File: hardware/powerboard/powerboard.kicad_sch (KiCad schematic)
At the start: 66 parts, among them J1 USB_B_Micro, J10 5V Header, J11 3V3 Header, J2 Boot, J3 Power, J4 Display, J5 Debug, J6 SPI_1, J7 UART_0, J8 I2C_0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

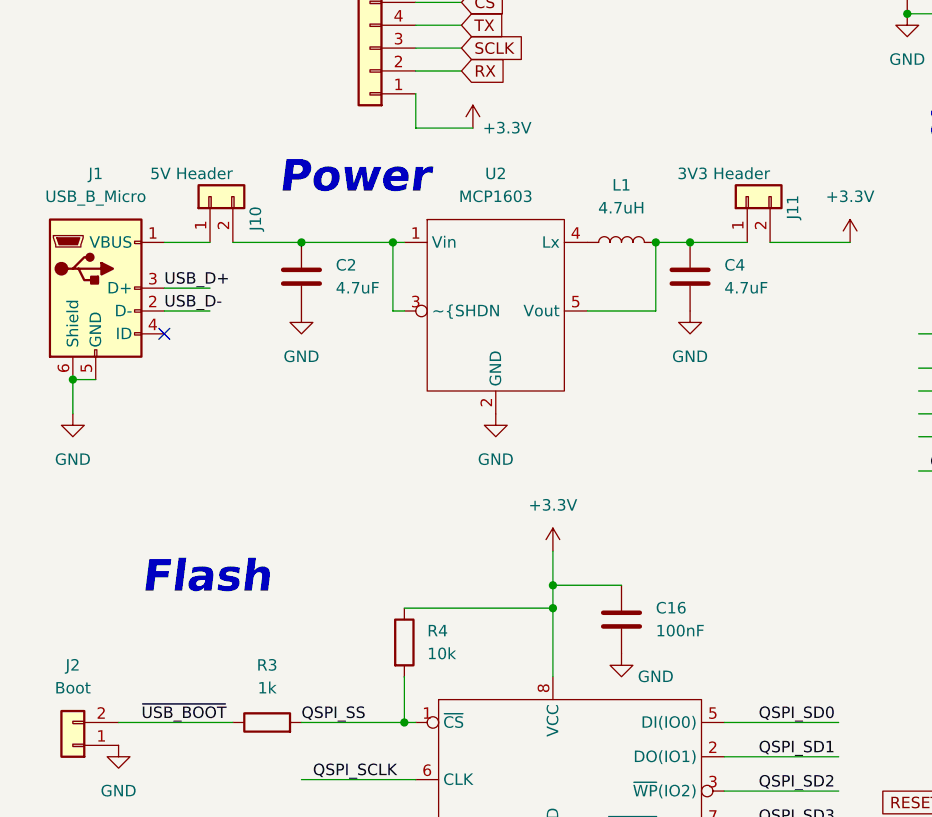
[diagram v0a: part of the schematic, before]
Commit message: JLC Capabilities Double Checked
Confirmed JLC Capabilities with Design Rules
CHECK SILKSCREEN RULES
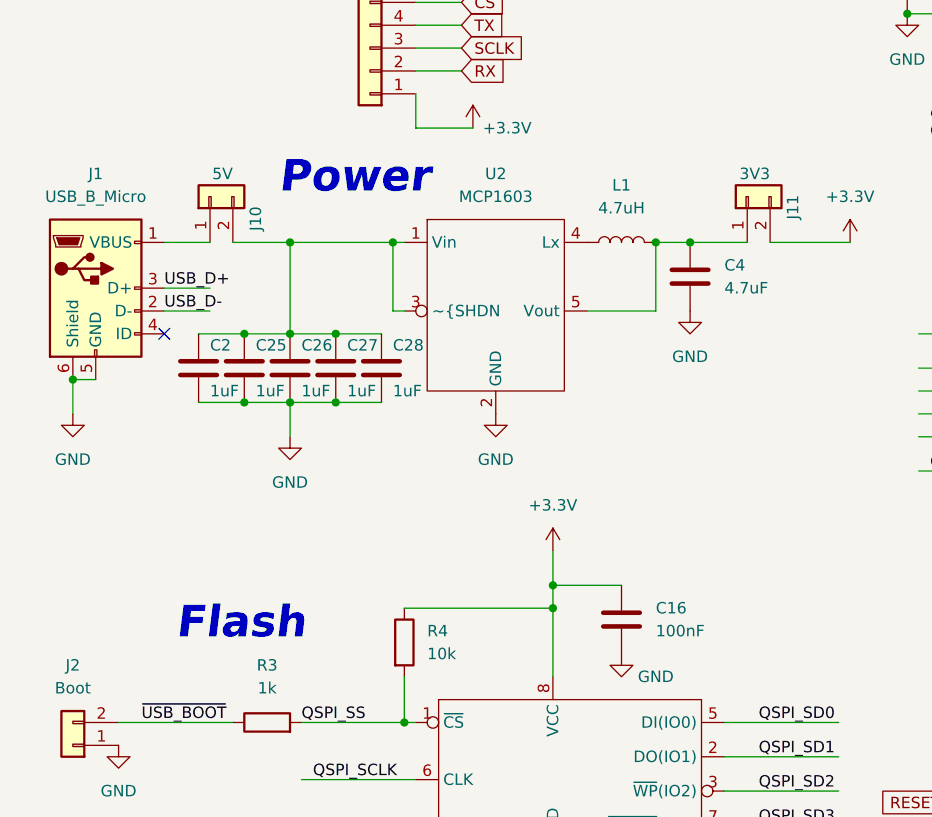
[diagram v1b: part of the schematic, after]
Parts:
- added C25, C26, C27, C28: 1uF, Capacitor_SMD:C_0805_2012Metric, symbol Device:C
- C2: value 4.7uF -> 1uF; footprint Capacitor_SMD:C_0603_1608Metric -> Capacitor_SMD:C_0805_2012Metric
- J10: value 5V Header -> 5V
- J11: value 3V3 Header -> 3V3
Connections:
- net GND: now also C25.2, C26.2, C27.2, C28.2
- net at C2.1, J10.2 (Pin_2), U2.1 (Vin)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: now also C25.1, C26.1, C27.1, C28.1

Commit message: MIDI Messages now only sent on Keypress
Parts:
- C4: footprint Capacitor_SMD:C_0603_1608Metric -> Capacitor_SMD:C_0805_2012Metric
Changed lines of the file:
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@@
       (effects (font (size 1.27 1.27)) (justify left))
     )
-    (property "Footprint" "Capacitor_SMD:C_0603_1608Metric" (id 2) (at 89.8652 69.85 0)
+    (property "Footprint" "Capacitor_SMD:C_0805_2012Metric" (id 2) (at 89.8652 69.85 0)
       (effects (font (size 1.27 1.27)) hide)
     )
@@
     )
     (path "/707b3643-99d8-4514-bbf8-587962bdcb4f"
-      (reference "C4") (unit 1) (value "4.7uF") (footprint "Capacitor_SMD:C_0603_1608Metric")
+      (reference "C4") (unit 1) (value "4.7uF") (footprint "Capacitor_SMD:C_0805_2012Metric")
     )
     (path "/62a559f3-0287-407e-b429-1597a5ab7b86"

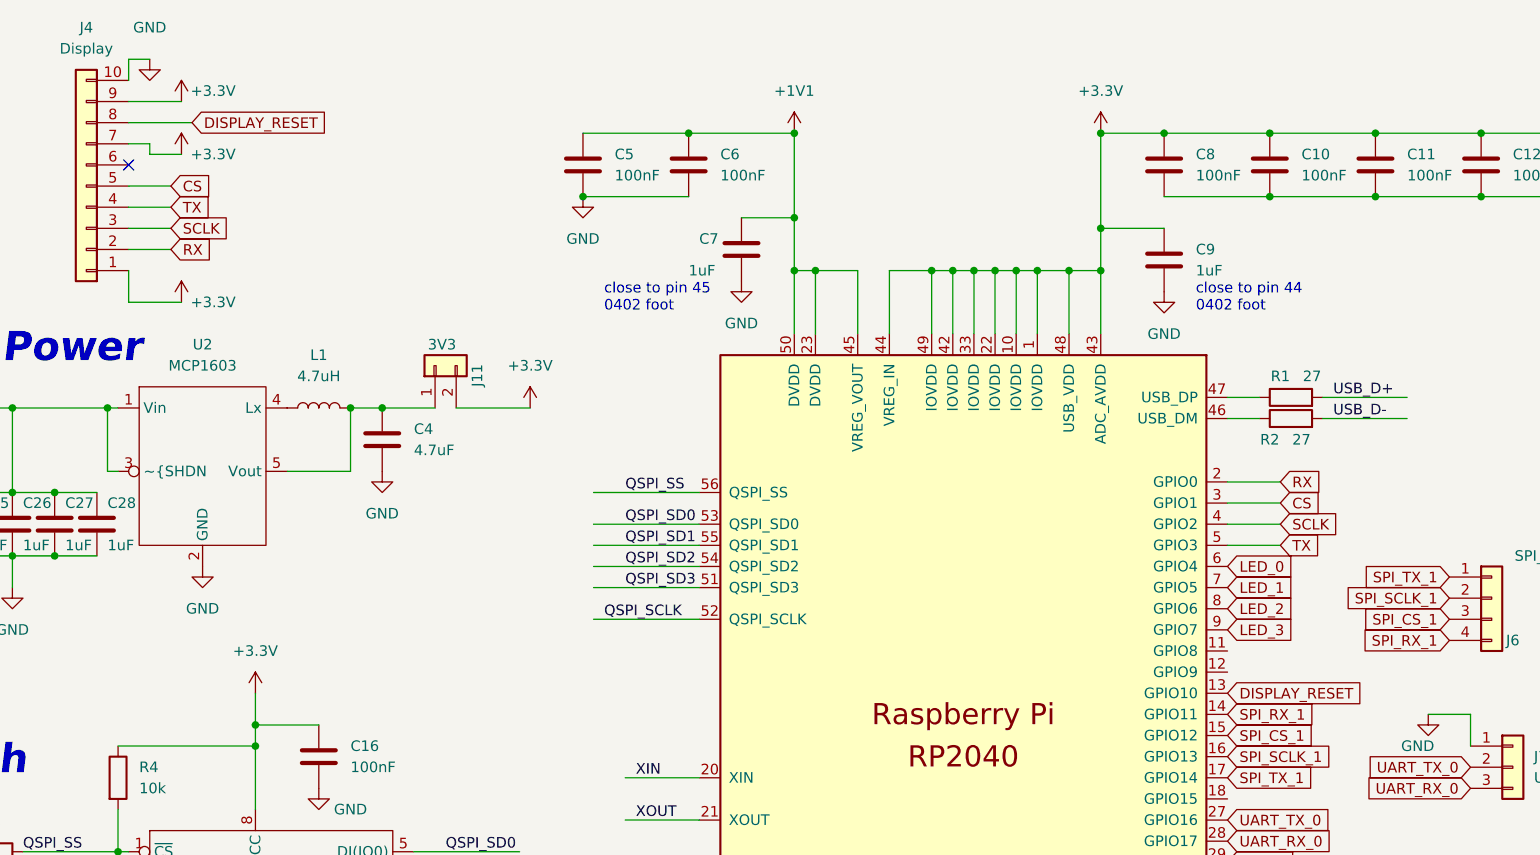
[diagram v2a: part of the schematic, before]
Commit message: GPIO Added for TFT_DC Display Pin
Connected GPIO 10 to TFT_DC Pin on Display Header
DISPLAY_RESET is now Connected to GPIO 9
pins.h updated accordingly
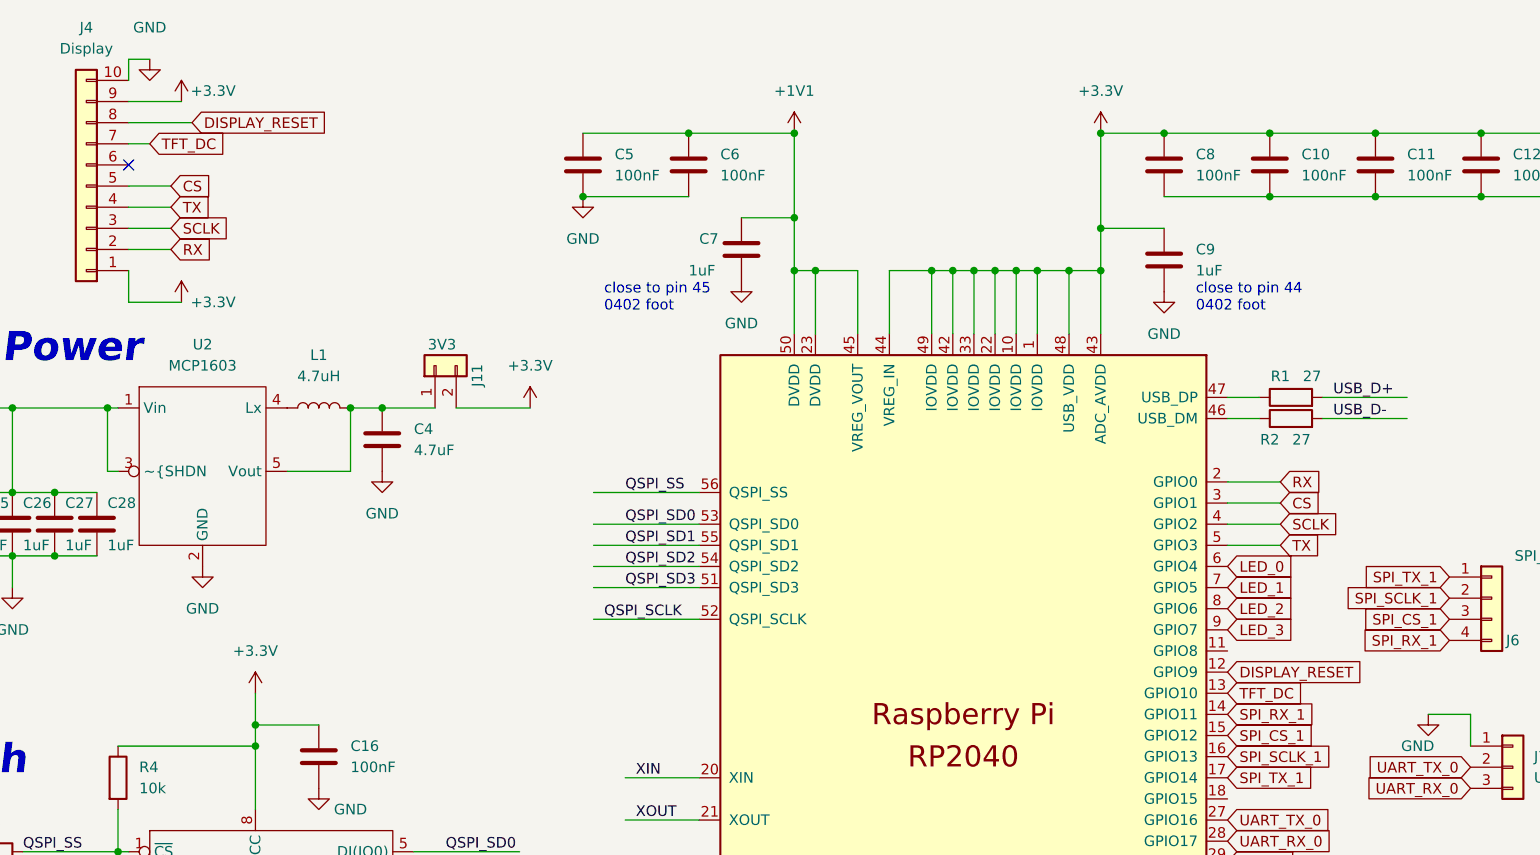
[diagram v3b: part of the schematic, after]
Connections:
- net +3.3V: no longer J4.7 (Pin_7)
- net DISPLAY_RESET: now also U3.12 (GPIO9); no longer U3.13 (GPIO10)
- new net TFT_DC: J4.7 (Pin_7), U3.13 (GPIO10)
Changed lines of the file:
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@@
-    (stroke (width 0) (type default) (color 0 0 0 0))
-  )
-  (wire (pts (xy 64.77 31.75) (xy 60.96 31.75))
     (stroke (width 0) (type default) (color 0 0 0 0))
   )
@@
   )
   (wire (pts (xy 22.86 152.4) (xy 27.94 152.4))
-    (stroke (width 0) (type default) (color 0 0 0 0))
-  )
-  (wire (pts (xy 60.96 31.75) (xy 60.96 30.48))
     (stroke (width 0) (type default) (color 0 0 0 0))
   )
@@
     )
   )
-  (global_label "DISPLAY_RESET" (shape input) (at 190.5 96.52 0) (fields_autoplaced)
-    (effects (font (size 1.27 1.27)) (justify left))
-    (property "Intersheet References" "${INTERSHEET_REFS}" (id 0) (at 207.1855 96.4406 0)
+  (global_label "DISPLAY_RESET" (shape input) (at 190.5 93.98 0) (fields_autoplaced)
+    (effects (font (size 1.27 1.27)) (justify left))
+    (property "Intersheet References" "${INTERSHEET_REFS}" (id 0) (at 207.1855 93.9006 0)
+      (effects (font (size 1.27 1.27)) (justify left) hide)
+    )
+  )
+  (global_label "TFT_DC" (shape input) (at 60.96 30.48 0) (fields_autoplaced)
+    (effects (font (size 1.27 1.27)) (justify left))
+    (property "Intersheet References" "${INTERSHEET_REFS}" (id 0) (at 69.9045 30.4006 0)
       (effects (font (size 1.27 1.27)) (justify left) hide)
     )
@@
     (property "Intersheet References" "${INTERSHEET_REFS}" (id 0) (at 16.8788 177.7206 0)
       (effects (font (size 1.27 1.27)) (justify right) hide)
+    )
+  )
+  (global_label "TFT_DC" (shape input) (at 190.5 96.52 0) (fields_autoplaced)
+    (effects (font (size 1.27 1.27)) (justify left))
+    (property "Intersheet References" "${INTERSHEET_REFS}" (id 0) (at 199.4445 96.4406 0)
+      (effects (font (size 1.27 1.27)) (justify left) hide)
     )
   )
@@
     (pin "2")
   )
-  (symbol (lib_id "power:+3.3V") (at 64.77 31.75 0) (unit 1)
-    (in_bom yes) (on_board yes)
-    (property "Reference" "#PWR06" (id 0) (at 64.77 35.56 0)
-      (effects (font (size 1.27 1.27)) hide)
-    )
-    (property "Value" "+3.3V" (id 1) (at 68.58 31.75 0))
-    (property "Footprint" "" (id 2) (at 64.77 31.75 0)
-      (effects (font (size 1.27 1.27)) hide)
-    )
-    (property "Datasheet" "" (id 3) (at 64.77 31.75 0)
-      (effects (font (size 1.27 1.27)) hide)
-    )
-    (pin "1")
-  )
   (symbol (lib_id "power:+3.3V") (at 34.29 22.86 0) (unit 1)
     (in_bom yes) (on_board yes) (fields_autoplaced)
@@
       (reference "#PWR05") (unit 1) (value "GND") (footprint "")
     )
-    (path "/f8107bfa-8926-48fc-a59a-d44657ce0461"
-      (reference "#PWR06") (unit 1) (value "+3.3V") (footprint "")
-    )
     (path "/550650b9-9aa6-4198-b86a-a5c8675143c2"

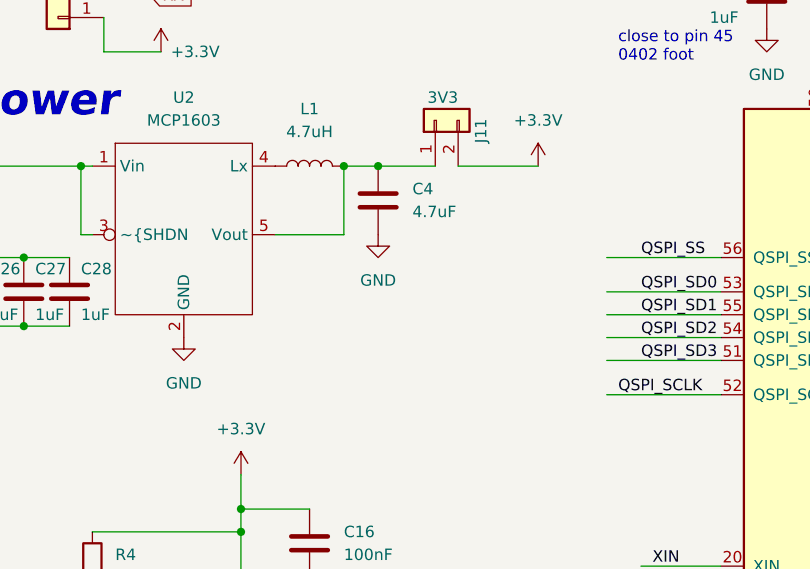
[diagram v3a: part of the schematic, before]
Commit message: powerboard adjustments, bom added
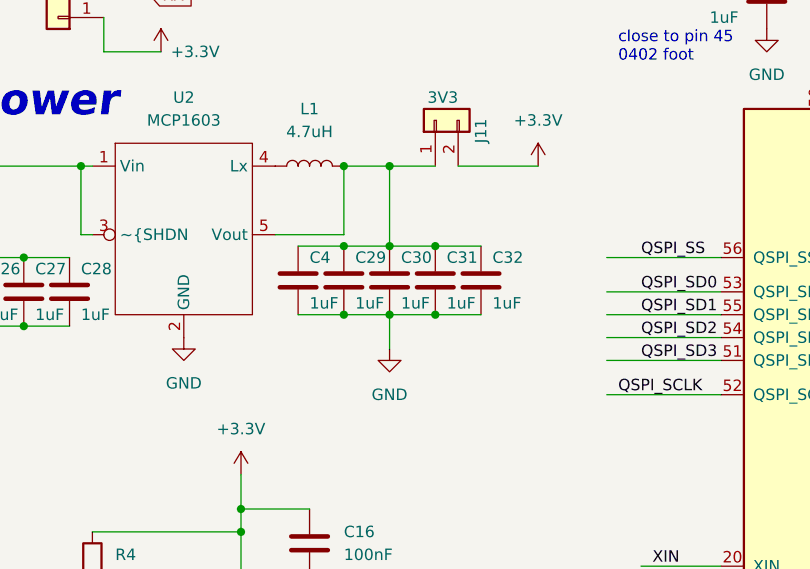
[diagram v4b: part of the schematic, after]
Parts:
- added C29, C30, C31, C32: 1uF, Capacitor_SMD:C_0805_2012Metric, symbol Device:C
- C4: value 4.7uF -> 1uF
- J7: footprint Connector_PinSocket_2.54mm:PinSocket_1x03_P2.54mm_Vertical -> Connector_PinHeader_2.54mm:PinHeader_1x03_P2.54mm_Vertical
- J8, J9: footprint Connector_PinSocket_2.54mm:PinSocket_1x04_P2.54mm_Vertical -> Connector_PinHeader_2.54mm:PinHeader_1x04_P2.54mm_Vertical
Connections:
- net GND: now also C29.2, C30.2, C31.2, C32.2
- net at C4.1, J11.1 (Pin_1), L1.2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: now also C29.1, C30.1, C31.1, C32.1

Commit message: Powerboard Output Files Pt.1
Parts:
- C1, C10, C11, C12, C13, C14, C15, C16, C23, C24, C5, C6, C8: LCSC (none) -> C307331
- C17, C18: LCSC (none) -> C1658
- C19, C20, C21: LCSC (none) -> C1588
- C2, C25, C26, C27, C28, C29, C30, C31, C32, C4: LCSC (none) -> C28323
- C22: LCSC (none) -> C440198
- C3: footprint Capacitor_SMD:C_0603_1608Metric -> Capacitor_SMD:C_0402_1005Metric; LCSC (none) -> C307331
- C7, C9: LCSC (none) -> C307413
- D1, D2, D3, D4: LCSC (none) -> C87326
- J1: LCSC (none) -> C132563
- J10, J11, J2: LCSC (none) -> C2905434
- J3: LCSC (none) -> C2905424
- J4: LCSC (none) -> C2905488
- J5, J7: LCSC (none) -> C2932698
- J6: LCSC (none) -> C492412
- J8, J9: LCSC (none) -> C2905345
- L1: LCSC (none) -> C701275
- R1, R2: LCSC (none) -> C25100
- R10, R11, R3, R5, R6, R7, R8, R9: LCSC (none) -> C21190
- R12, R13, R14, R4: LCSC (none) -> C25804
- R15, R16, R17, R18: LCSC (none) -> C23138
- SW1, SW2, SW3: LCSC (none) -> C428628
- SW4: LCSC (none) -> C278348
- U2: LCSC (none) -> C150803
- U3: LCSC (none) -> C9900024873
- U4: LCSC (none) -> C2613930
- Y1: LCSC (none) -> C133334
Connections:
- net +3.3V: now also C29.1, C30.1, C31.1, C32.1, C4.1, J11.1 (Pin_1), L1.2, U2.5 (Vout)
- no-connect marks 3 -> 7
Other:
- company: (none) -> Landyn Francis & Jacob Mealey
- title: (none) -> MIDI Keyboard: Brain Board

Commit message: Gerbers and pick and place generated
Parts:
- removed J3: Power, Connector_PinHeader_2.54mm:PinHeader_1x02_P2.54mm_Horizontal, symbol Connector_Generic:Conn_01x02
- removed J6: SPI_1, Connector_PinHeader_2.54mm:PinHeader_1x04_P2.54mm_Horizontal, symbol Connector_Generic:Conn_01x04
- added J3: Keysboard Header, Connector_PinHeader_2.54mm:PinHeader_1x06_P2.54mm_Horizontal, symbol Connector_Generic:Conn_01x06
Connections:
- net +3.3V: now also J3.2 (Pin_2)
- net GND: now also J3.1 (Pin_1)
- net SPI_CS_1: now also J3.5 (Pin_5)
- net SPI_RX_1: now also J3.6 (Pin_6)
- net SPI_SCLK_1: now also J3.4 (Pin_4)
- net SPI_TX_1: now also J3.3 (Pin_3)

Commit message: Footprint adjusted for W25QJVSIM FLASH
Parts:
- J8, J9: LCSC C2905345 -> C2905435
- U4: footprint Package_SO:SOIC-8_7.5x5.85mm_P1.27mm -> Package_SO:SOIC-8W_5.3x5.3mm_P1.27mm
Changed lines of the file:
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@@
       (effects (font (size 1.27 1.27)) hide)
     )
-    (property "LCSC" "C2905345" (id 4) (at 224.79 151.13 0)
+    (property "LCSC" "C2905435" (id 4) (at 224.79 151.13 0)
       (effects (font (size 1.27 1.27)) hide)
     )
@@
       (effects (font (size 1.27 1.27)) hide)
     )
-    (property "LCSC" "C2905345" (id 4) (at 228.6 125.73 0)
+    (property "LCSC" "C2905435" (id 4) (at 228.6 125.73 0)
       (effects (font (size 1.27 1.27)) hide)
     )
@@
     (property "Reference" "U4" (id 0) (at 62.23 130.81 0))
     (property "Value" "W25Q128JVSIM" (id 1) (at 85.09 130.81 0))
-    (property "Footprint" "Package_SO:SOIC-8_7.5x5.85mm_P1.27mm" (id 2) (at 73.66 125.73 0)
+    (property "Footprint" "Package_SO:SOIC-8W_5.3x5.3mm_P1.27mm" (id 2) (at 73.66 125.73 0)
       (effects (font (size 1.27 1.27)) hide)
     )
@@
     )
     (path "/70170b34-5bfa-4c43-b44d-5d4dc37abfec"
-      (reference "U4") (unit 1) (value "W25Q128JVSIM") (footprint "Package_SO:SOIC-8_7.5x5.85mm_P1.27mm")
+      (reference "U4") (unit 1) (value "W25Q128JVSIM") (footprint "Package_SO:SOIC-8W_5.3x5.3mm_P1.27mm")
     )
     (path "/ba8e6830-321e-44a3-ba32-74f2320fc32f"

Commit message: Trying to finalize Powerboard PCB
JLC is being bitchy about the RP2040 and MCP1603, the parts aren't showing up in the part viewer preview window and they are "unselected" for assembly because "coordinate data cannot be found". Very worrying. but as detailed in my message on Discord, I think I have a solution.
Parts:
- U3: footprint RP2040_minimal:RP2040-QFN-56 -> Package_DFN_QFN:QFN-56-1EP_7x7mm_P0.4mm_EP3.2x3.2mm
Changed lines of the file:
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@@
       (effects (font (size 1.27 1.27)) (justify left))
     )
-    (property "Footprint" "RP2040_minimal:RP2040-QFN-56" (id 2) (at 139.7 104.14 0)
+    (property "Footprint" "Package_DFN_QFN:QFN-56-1EP_7x7mm_P0.4mm_EP3.2x3.2mm" (id 2) (at 139.7 104.14 0)
       (effects (font (size 1.27 1.27)) hide)
     )
@@
     )
     (path "/26309b49-910b-44e4-84c1-8d3b7988a81c"
-      (reference "U3") (unit 1) (value "RP2040") (footprint "RP2040_minimal:RP2040-QFN-56")
+      (reference "U3") (unit 1) (value "RP2040") (footprint "Package_DFN_QFN:QFN-56-1EP_7x7mm_P0.4mm_EP3.2x3.2mm")
     )
     (path "/70170b34-5bfa-4c43-b44d-5d4dc37abfec"
